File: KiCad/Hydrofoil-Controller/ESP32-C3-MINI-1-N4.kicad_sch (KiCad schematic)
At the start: 20 parts, among them U1 ESP32-C3-MINI-1-N4

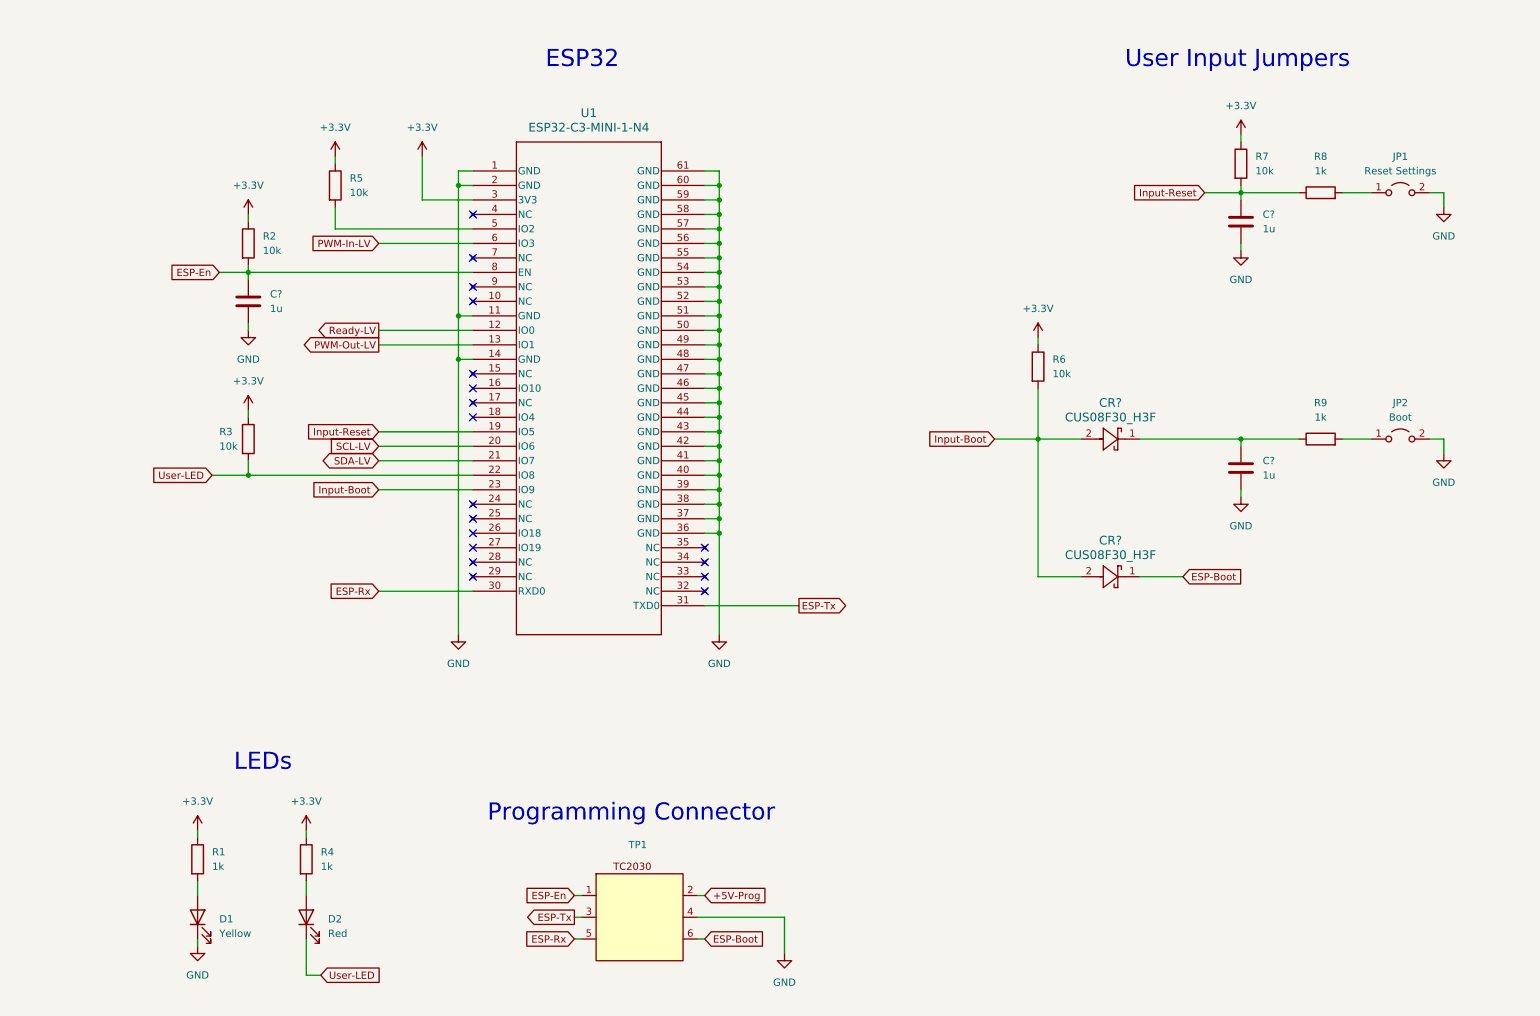
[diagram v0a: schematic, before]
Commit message: Remove ADC from PCB
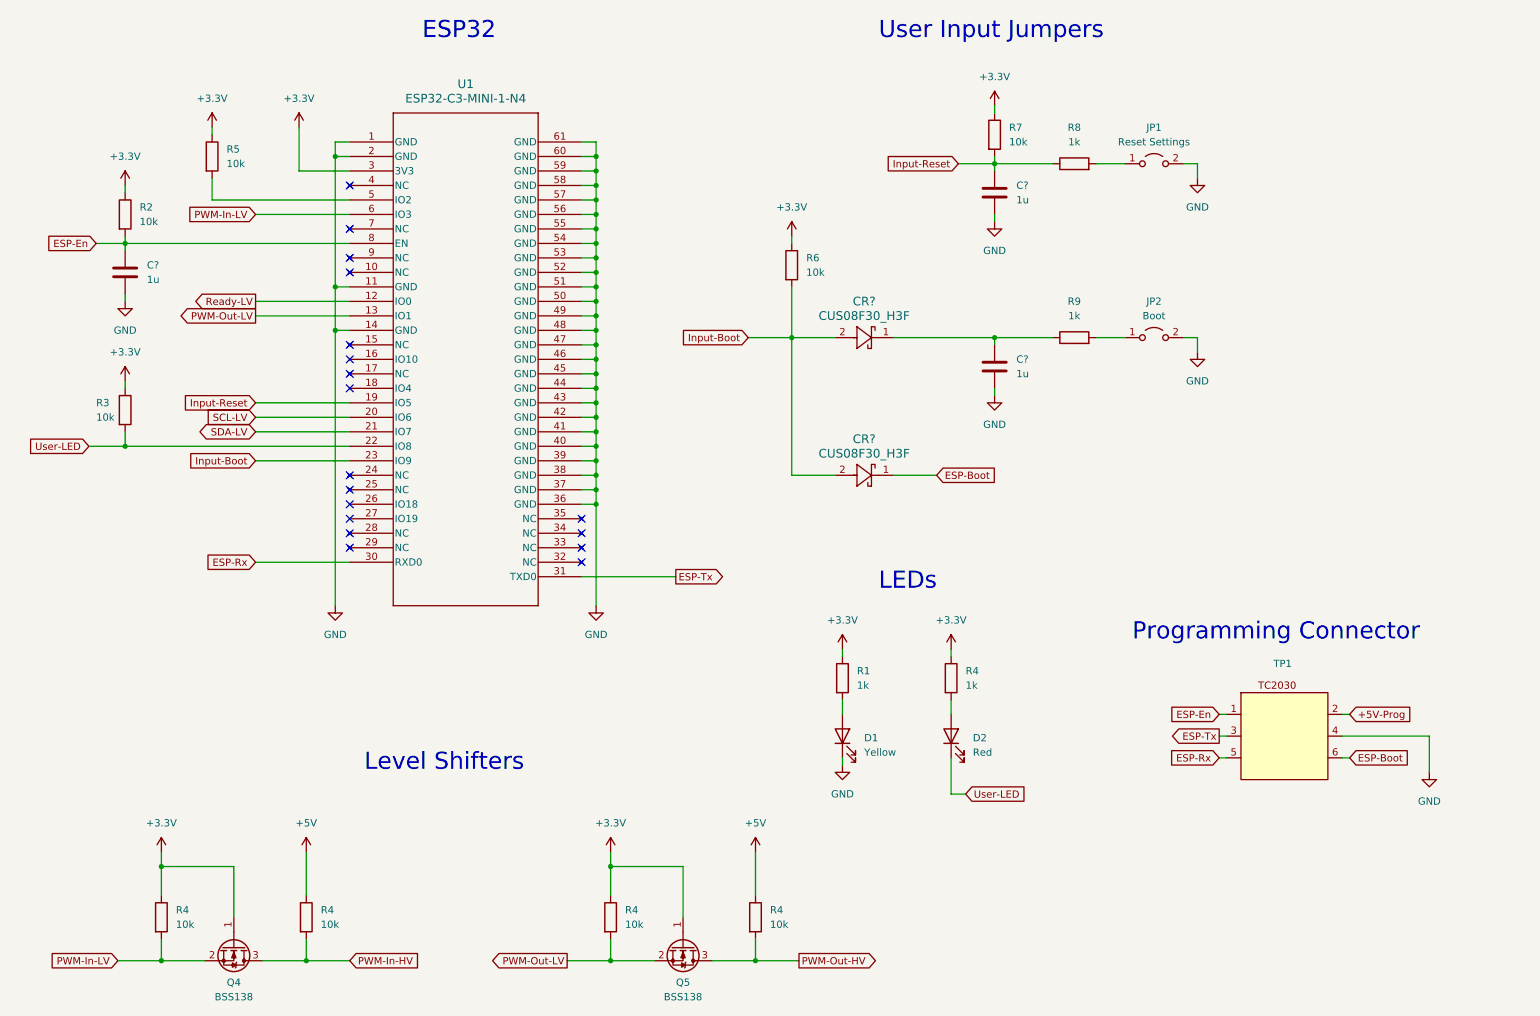
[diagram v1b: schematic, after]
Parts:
- added Q4, Q5: BSS138, Package_TO_SOT_SMD:SOT-23, symbol Transistor_FET:BSS138
- added R4 (x4): 10k, Resistor_SMD:R_0402_1005Metric_Pad0.72x0.64mm_HandSolder, symbol Device:R
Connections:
- net +3.3V: now also Q4.1 (G), Q5.1 (G), R4.1, R4.1
- net PWM-In-LV: now also Q4.2 (S), R4.2
- net PWM-Out-LV: now also Q5.2 (S), R4.2
- new net +5V: R4.1, R4.1
- new net PWM-In-HV: Q4.3 (D), R4.2
- new net PWM-Out-HV: Q5.3 (D), R4.2
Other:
- note added: "Level Shifters"
- moved on the sheet: C?, CR?, D1, D2, JP1, JP2, R1, R2, R3, R4, R5, R6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
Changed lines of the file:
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@@
     (rev "v1.1")
     (company "Tamás Nagy")
+    (comment 1 "ADC removed, capacitance measurement added")
   )

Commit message: Add capacitance measurement to the PCB
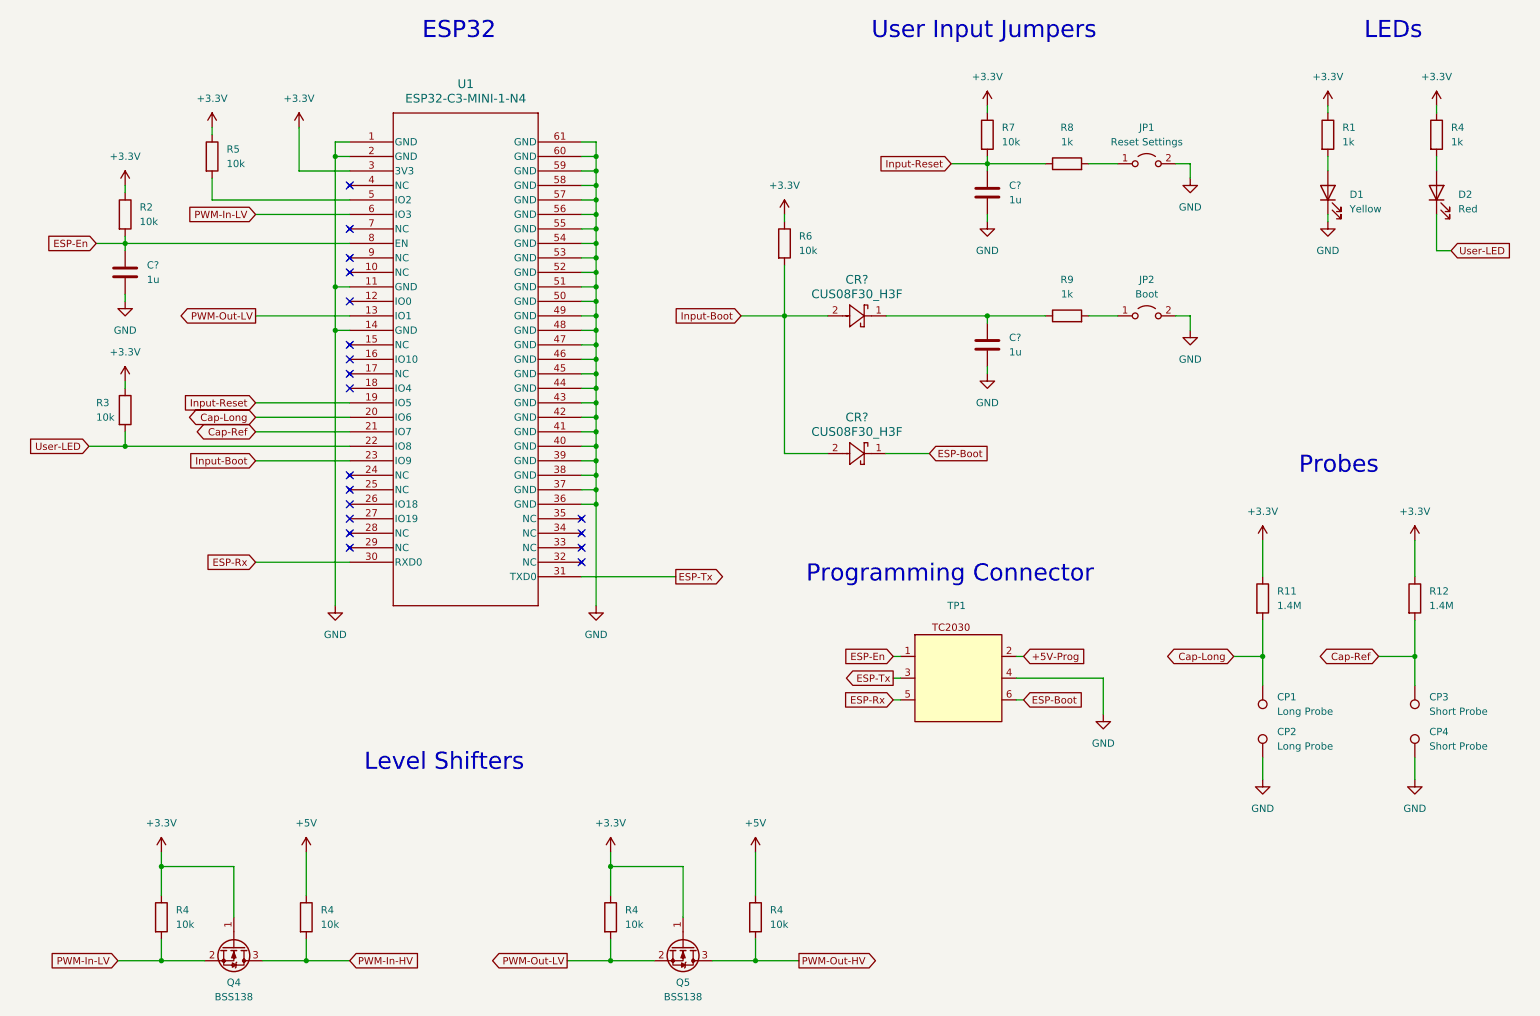
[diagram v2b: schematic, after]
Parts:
- added CP1, CP2: Long Probe, TestPoint:TestPoint_Pad_D2.0mm, symbol Connector:TestPoint
- added CP3, CP4: Short Probe, TestPoint:TestPoint_Pad_D2.0mm, symbol Connector:TestPoint
- added R11, R12: 1.4M, Resistor_SMD:R_0402_1005Metric_Pad0.72x0.64mm_HandSolder, symbol Device:R
- JP1, JP2, TP1: MPN (none) -> No Part Required
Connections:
- net +3.3V: now also R11.1, R12.1
- net GND: now also CP2.1, CP4.1
- net Ready-LV: no longer names the net of U1.12 (IO0)
- net SCL-LV renamed Cap-Long
- net Cap-Long: now also CP1.1, R11.2
- net SDA-LV renamed Cap-Ref
- net Cap-Ref: now also CP3.1, R12.2
- no-connect marks 18 -> 19
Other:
- note added: "Probes"
- moved on the sheet: C?, CR?, D1, D2, JP1, JP2, R1, R4, R6, R7, R8, R9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
